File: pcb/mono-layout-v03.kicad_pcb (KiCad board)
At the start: 2 copper layers, 100 x 90 mm, 26 parts, among them J1 L RCA, J2 L TEST OUT, J5 INTERNAL PSU, U1 LM3886T

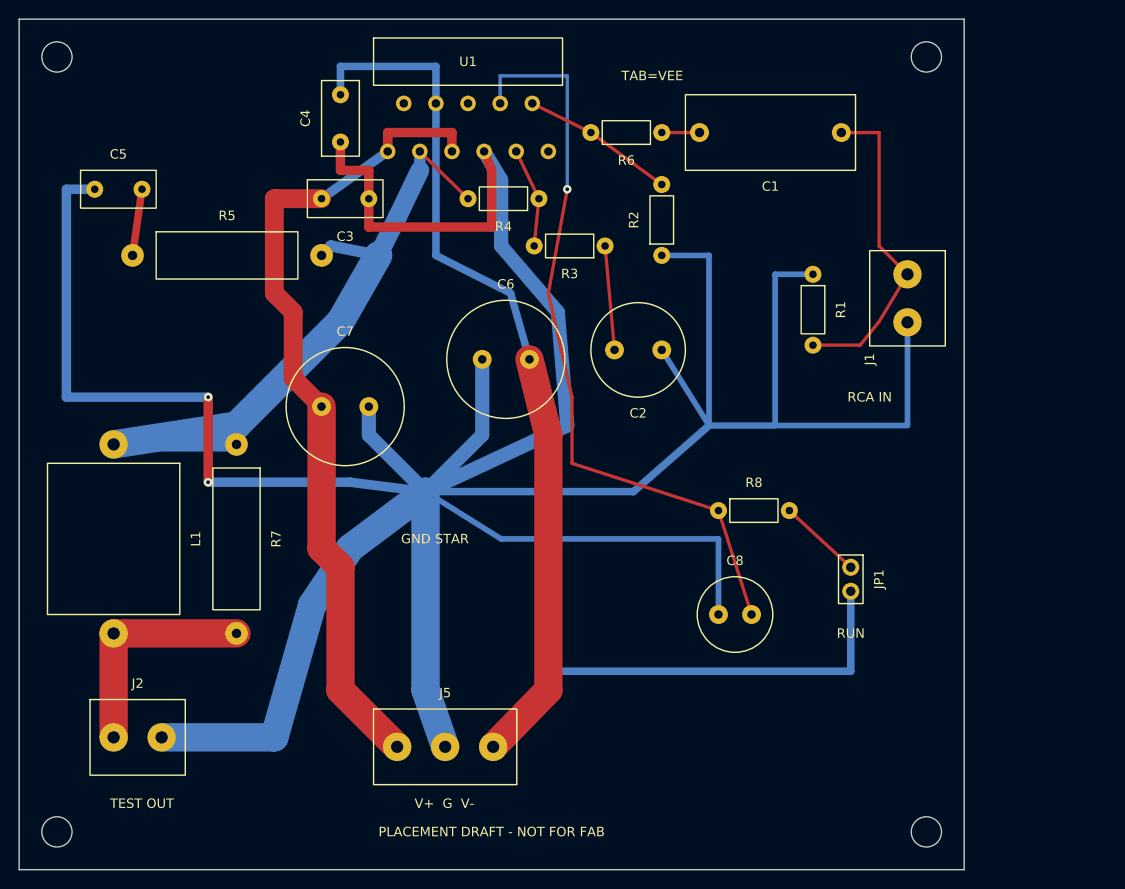
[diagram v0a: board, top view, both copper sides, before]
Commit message: rebuild: 原理圖與 PCB 以本機 KiCad 10.0.6 重建，兩板 DRC 0 違規
- 原理圖：ERC 0；verify_electrical 期望值改為實購 100V／0.6W 後通過
- PCB：修正首輪 DRC（C2/R1 保留區重疊、U1 絲印字高與壓字）與回地分組碰觸
  （靜音回流改經 via_mute_ret），DRC 0 違規 0 未連通，verify/analyze/test 通過
- 工具：KiCad 在 Windows 寫出的 CRLF 轉 LF 後才雜湊；雜湊路徑改 as_posix()
- 文件同步；pcb/inspection-v03 與 docs/diagrams 尚未重建

Co-Authored-By: Claude Opus 5.5 (1M context) <noreply@anthropic.com>
Claude-Session: https://claude.ai/code/session_01DerP5HjoiFxZ4hz4f3ygqt
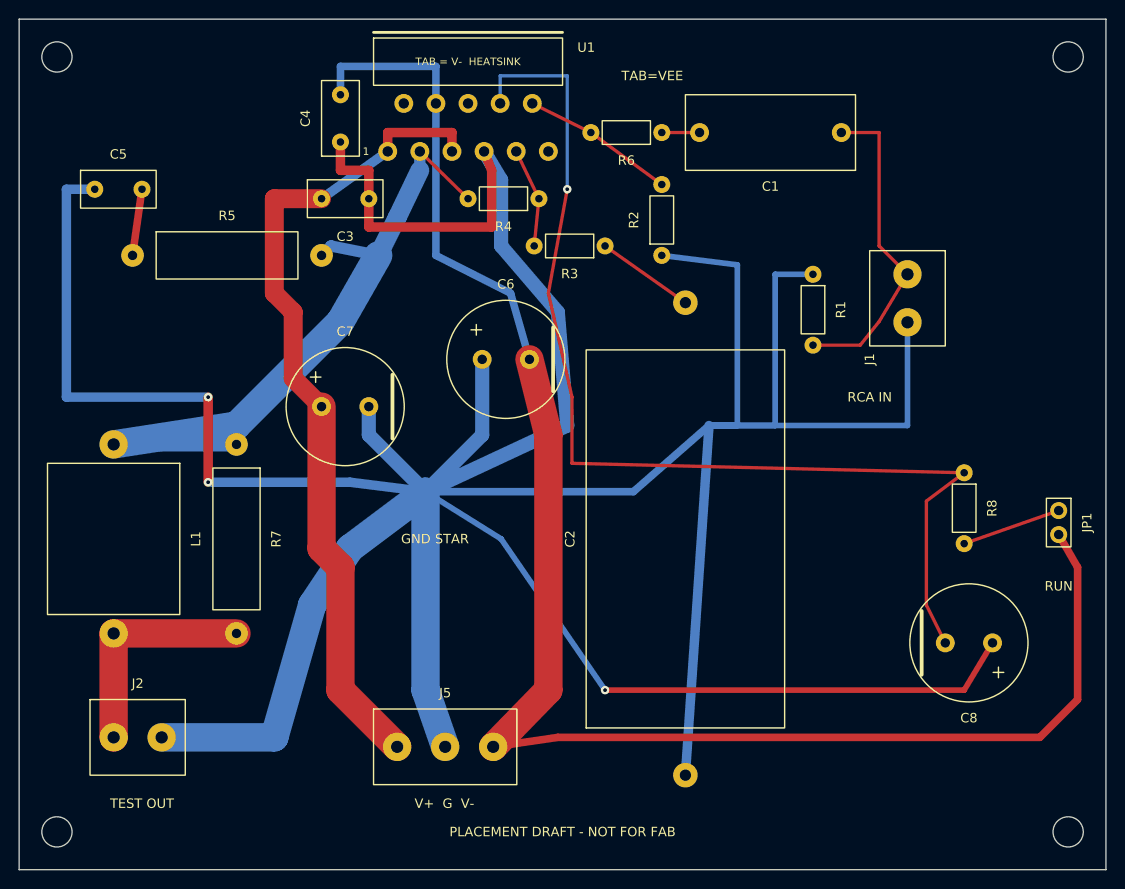
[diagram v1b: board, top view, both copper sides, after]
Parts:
- C1: value 2.2u / 63V film -> 2.2u / 100V film
- C2: footprint BP_D10_P5 -> BP_Axial_L40_D20_P50
- C3, C4: value 100n / 63V -> 100n / 100V
- C8: value 100u / 63V -> 100u / 100V; footprint CP_D8_P3.5 -> CP_D12.5_P5
- R8: value 22k / 0.25W -> 22k / 0.6W
- moved C2 45.1 mm to (70.5, 80.0), turned to 90 degrees
- moved C8 29.2 mm to (103.0, 66.0), turned to 180 degrees
- moved R8 26.3 mm to (100.0, 48.0), turned to -90 degrees
- moved JP1 22.8 mm to (110.0, 52.0)
- moved H2 15.0 mm to (111.0, 4.00)
- moved H4 15.0 mm to (111.0, 86.0)
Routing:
- net GND: track 417.0 -> 481.9 mm, vias 2 -> 3
- net L_MUTE: track 79.3 -> 113.5 mm
- net VEE: track 142.8 -> 174.4 mm
- net L_RUN: track 8.85 -> 10.6 mm
- net L_FB_AC: track 11.0 -> 10.4 mm
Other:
- board size 100 x 90 mm -> 115 x 90 mm
